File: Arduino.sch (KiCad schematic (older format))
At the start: 0 parts

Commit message: Add projects simples and adding a sun Sch
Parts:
- added BT?: Battery, symbol Device:Battery
- added C? (x2): C, symbol Device:C
- added C?: CP, symbol Device:CP
- added D?: LED, symbol Device:LED
- added R? (x2): R, symbol Device:R
- added U?: 24LC1025, symbol Memory_EEPROM:24LC1025
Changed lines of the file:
@@
 $Descr A4 11693 8268
 encoding utf-8
-Sheet 1 1
+Sheet 1 2
 Title "Arduino"
 Date "2021-10-07"
@@
 Comment4 ""
 $EndDescr
+$Comp
+L Device:Battery BT?
+U 1 1 615F0300
+P 7050 3050
+F 0 "BT?" H 7158 3096 50  0000 L CNN
+F 1 "Battery" H 7158 3005 50  0000 L CNN
+F 2 "" V 7050 3110 50  0001 C CNN
+F 3 "~" V 7050 3110 50  0001 C CNN
+	1    7050 3050
+	1    0    0    -1
+$EndComp
+$Comp
+L Device:C C?
+U 1 1 615F14AB
+P 5450 1750
+F 0 "C?" H 5565 1796 50  0000 L CNN
+F 1 "C" H 5565 1705 50  0000 L CNN
+F 2 "" H 5488 1600 50  0001 C CNN
+F 3 "~" H 5450 1750 50  0001 C CNN
+	1    5450 1750
+	1    0    0    -1
+$EndComp
+$Comp
+L Device:C C?
+U 1 1 615F1778
+P 5450 2400
+F 0 "C?" H 5565 2446 50  0000 L CNN
+F 1 "C" H 5565 2355 50  0000 L CNN
+F 2 "" H 5488 2250 50  0001 C CNN
+F 3 "~" H 5450 2400 50  0001 C CNN
+	1    5450 2400
+	1    0    0    -1
+$EndComp
+$Comp
+L Device:CP C?
+U 1 1 615F1B97
+P 6350 1800
+F 0 "C?" H 6468 1846 50  0000 L CNN
+F 1 "CP" H 6468 1755 50  0000 L CNN
+F 2 "" H 6388 1650 50  0001 C CNN
+F 3 "~" H 6350 1800 50  0001 C CNN
+	1    6350 1800
+	1    0    0    -1
+$EndComp
+$Comp
+L Device:LED D?
+U 1 1 615F28FB
+P 7600 1750
+F 0 "D?" H 7593 1967 50  0000 C CNN
+F 1 "LED" H 7593 1876 50  0000 C CNN
+F 2 "" H 7600 1750 50  0001 C CNN
+F 3 "~" H 7600 1750 50  0001 C CNN
+	1    7600 1750
+	1    0    0    -1
+$EndComp
+$Comp
+L Device:R R?
+U 1 1 615F2E86
+P 8250 1950
+F 0 "R?" H 8320 1996 50  0000 L CNN
+F 1 "R" H 8320 1905 50  0000 L CNN
+F 2 "" V 8180 1950 50  0001 C CNN
+F 3 "~" H 8250 1950 50  0001 C CNN
+	1    8250 1950
+	1    0    0    -1
+$EndComp
+$Comp
+L Device:R R?
+U 1 1 615F3234
+P 8250 2400
+F 0 "R?" H 8320 2446 50  0000 L CNN
+F 1 "R" H 8320 2355 50  0000 L CNN
+F 2 "" V 8180 2400 50  0001 C CNN
+F 3 "~" H 8250 2400 50  0001 C CNN
+	1    8250 2400
+	1    0    0    -1
+$EndComp
+$Comp
+L Memory_EEPROM:24LC1025 U?
+U 1 1 615F39A8
+P 9550 1950
+F 0 "U?" H 9550 2431 50  0000 C CNN
+F 1 "24LC1025" H 9550 2340 50  0000 C CNN
+F 2 "" H 9550 1950 50  0001 C CNN
+F 3 "http://ww1.microchip.com/downloads/en/DeviceDoc/21941B.pdf" H 9550 1950 50  0001 C CNN
+	1    9550 1950
+	1    0    0    -1
+$EndComp
+$Sheet
+S 8250 3000 2950 3550
+U 615F48EA
+F0 "Connectors" 50
+F1 "connectors.sch" 50
+$EndSheet
 $EndSCHEMATC

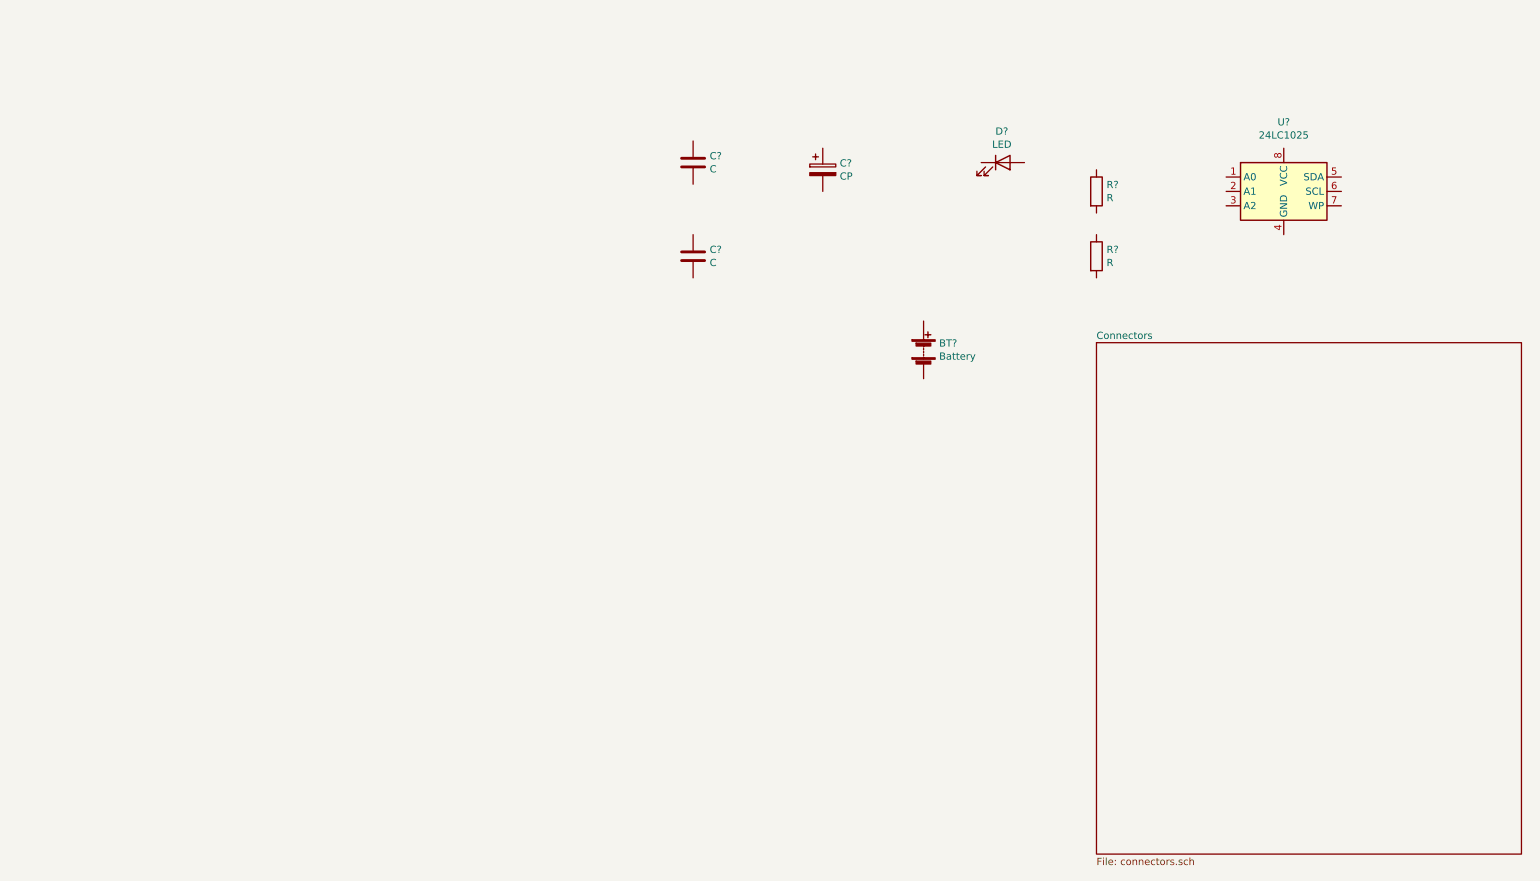
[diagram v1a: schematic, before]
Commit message: Complete the association with footprint
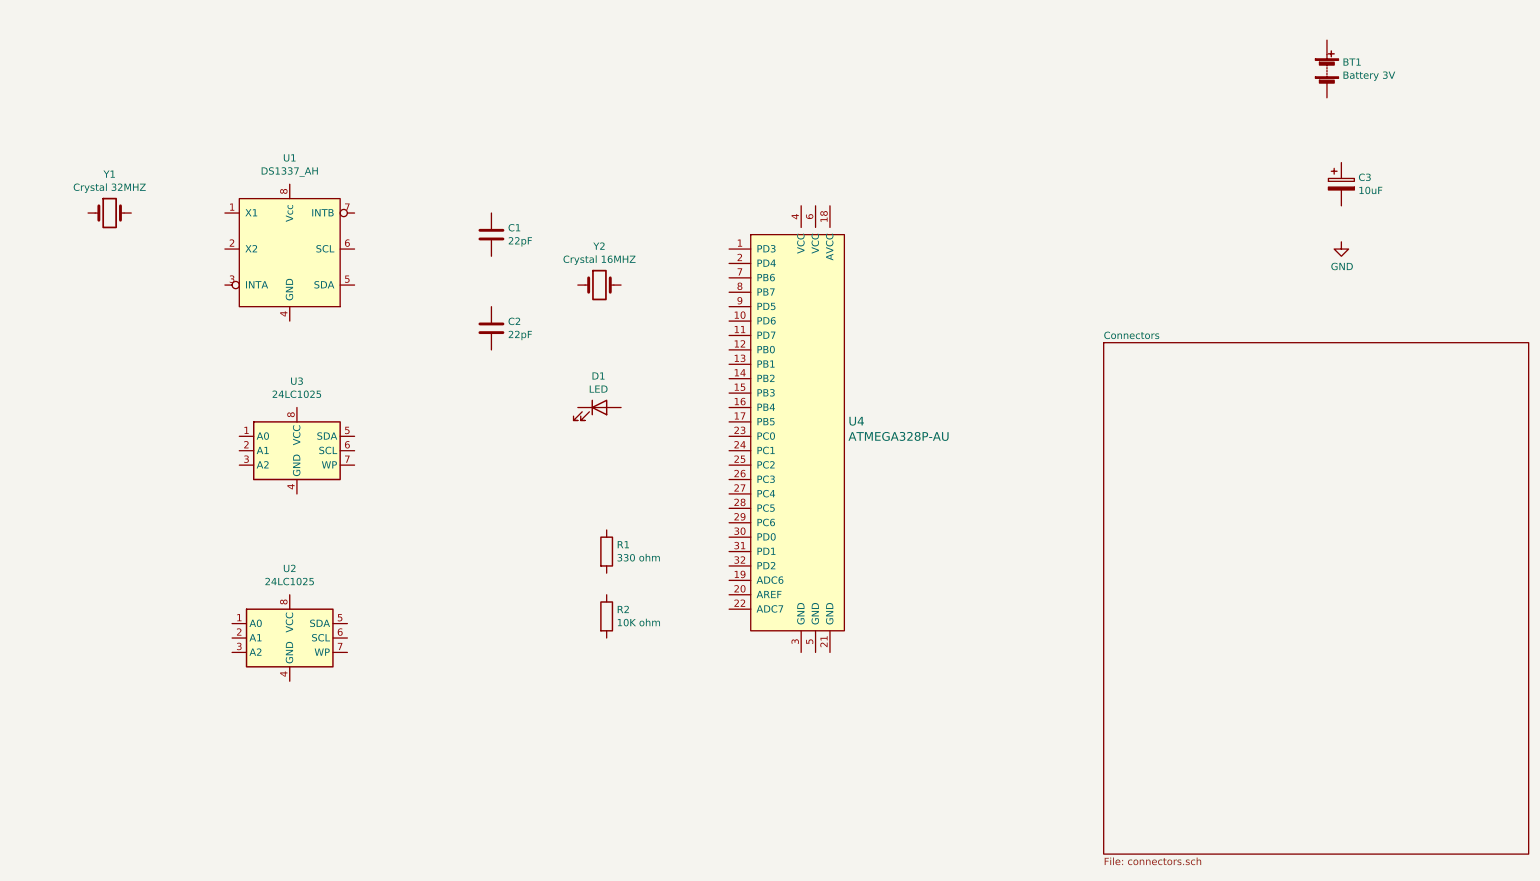
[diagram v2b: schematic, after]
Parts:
- added U1: DS1337_AH, Package_SO:SO-8_5.3x6.2mm_P1.27mm, symbol Ahmad_Library:DS1337_AH
- added U2: 24LC1025, Package_SO:SOIC-8_5.23x5.23mm_P1.27mm, symbol Memory_EEPROM:24LC1025
- added U4: ATMEGA328P-AU, digikey-footprints:TQFP-32_7x7mm, symbol dk_Embedded-Microcontrollers:ATMEGA328P-AU
- added Y1: Crystal 32MHZ, Crystal:Crystal_SMD_MicroCrystal_CC7V-T1A-2Pin_3.2x1.5mm, symbol Device:Crystal
- added Y2: Crystal 16MHZ, Crystal:Crystal_SMD_5032-2Pin_5.0x3.2mm_HandSoldering, symbol Device:Crystal
- BT1: renamed from BT?; value Battery -> Battery 3V; footprint (none) -> Connector_PinHeader_2.54mm:PinHeader_1x02_P2.54mm_Vertical
- C1, C2: renamed from C?; value C -> 22pF; footprint (none) -> Capacitor_SMD:C_0805_2012Metric_Pad1.18x1.45mm_HandSolder
- C3: renamed from C?; value CP -> 10uF; footprint (none) -> Capacitor_SMD:C_0805_2012Metric_Pad1.18x1.45mm_HandSolder
- D1: renamed from D?; footprint (none) -> LED_SMD:LED_0805_2012Metric_Pad1.15x1.40mm_HandSolder
- R1: renamed from R?; value R -> 330 ohm; footprint (none) -> Resistor_SMD:R_0805_2012Metric_Pad1.20x1.40mm_HandSolder
- R2: renamed from R?; value R -> 10K ohm; footprint (none) -> Resistor_SMD:R_0805_2012Metric_Pad1.20x1.40mm_HandSolder
- U3: renamed from U?; footprint (none) -> Package_SO:SOIC-8_5.23x5.23mm_P1.27mm
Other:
- moved on the sheet: BT1, C1, C2, C3, D1, R1, R2, U3
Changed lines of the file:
@@
 $EndDescr
 $Comp
-L Device:Battery BT?
+L Device:Battery BT1
 U 1 1 615F0300
-P 7050 3050
-F 0 "BT?" H 7158 3096 50  0000 L CNN
-F 1 "Battery" H 7158 3005 50  0000 L CNN
-F 2 "" V 7050 3110 50  0001 C CNN
-F 3 "~" V 7050 3110 50  0001 C CNN
-	1    7050 3050
+P 9850 1100
+F 0 "BT1" H 9958 1146 50  0000 L CNN
+F 1 "Battery 3V" H 9958 1055 50  0000 L CNN
+F 2 "Connector_PinHeader_2.54mm:PinHeader_1x02_P2.54mm_Vertical" V 9850 1160 50  0001 C CNN
+F 3 "~" V 9850 1160 50  0001 C CNN
+	1    9850 1100
 	1    0    0    -1
 $EndComp
 $Comp
-L Device:C C?
+L Device:C C1
 U 1 1 615F14AB
-P 5450 1750
-F 0 "C?" H 5565 1796 50  0000 L CNN
-F 1 "C" H 5565 1705 50  0000 L CNN
-F 2 "" H 5488 1600 50  0001 C CNN
-F 3 "~" H 5450 1750 50  0001 C CNN
-	1    5450 1750
+P 4050 2250
+F 0 "C1" H 4165 2296 50  0000 L CNN
+F 1 "22pF" H 4165 2205 50  0000 L CNN
+F 2 "Capacitor_SMD:C_0805_2012Metric_Pad1.18x1.45mm_HandSolder" H 4088 2100 50  0001 C CNN
+F 3 "~" H 4050 2250 50  0001 C CNN
+	1    4050 2250
 	1    0    0    -1
 $EndComp
 $Comp
-L Device:C C?
+L Device:C C2
 U 1 1 615F1778
-P 5450 2400
-F 0 "C?" H 5565 2446 50  0000 L CNN
-F 1 "C" H 5565 2355 50  0000 L CNN
-F 2 "" H 5488 2250 50  0001 C CNN
-F 3 "~" H 5450 2400 50  0001 C CNN
-	1    5450 2400
+P 4050 2900
+F 0 "C2" H 4165 2946 50  0000 L CNN
+F 1 "22pF" H 4165 2855 50  0000 L CNN
+F 2 "Capacitor_SMD:C_0805_2012Metric_Pad1.18x1.45mm_HandSolder" H 4088 2750 50  0001 C CNN
+F 3 "~" H 4050 2900 50  0001 C CNN
+	1    4050 2900
 	1    0    0    -1
 $EndComp
 $Comp
-L Device:CP C?
+L Device:CP C3
 U 1 1 615F1B97
-P 6350 1800
-F 0 "C?" H 6468 1846 50  0000 L CNN
-F 1 "CP" H 6468 1755 50  0000 L CNN
-F 2 "" H 6388 1650 50  0001 C CNN
-F 3 "~" H 6350 1800 50  0001 C CNN
-	1    6350 1800
+P 9950 1900
+F 0 "C3" H 10068 1946 50  0000 L CNN
+F 1 "10uF" H 10068 1855 50  0000 L CNN
+F 2 "Capacitor_SMD:C_0805_2012Metric_Pad1.18x1.45mm_HandSolder" H 9988 1750 50  0001 C CNN
+F 3 "~" H 9950 1900 50  0001 C CNN
+	1    9950 1900
 	1    0    0    -1
 $EndComp
 $Comp
-L Device:LED D?
+L Device:LED D1
 U 1 1 615F28FB
-P 7600 1750
-F 0 "D?" H 7593 1967 50  0000 C CNN
-F 1 "LED" H 7593 1876 50  0000 C CNN
-F 2 "" H 7600 1750 50  0001 C CNN
-F 3 "~" H 7600 1750 50  0001 C CNN
-	1    7600 1750
+P 4800 3450
+F 0 "D1" H 4793 3667 50  0000 C CNN
+F 1 "LED" H 4793 3576 50  0000 C CNN
+F 2 "LED_SMD:LED_0805_2012Metric_Pad1.15x1.40mm_HandSolder" H 4800 3450 50  0001 C CNN
+F 3 "~" H 4800 3450 50  0001 C CNN
+	1    4800 3450
 	1    0    0    -1
 $EndComp
 $Comp
-L Device:R R?
-U 1 1 615F2E86
-P 8250 1950
-F 0 "R?" H 8320 1996 50  0000 L CNN
-F 1 "R" H 8320 1905 50  0000 L CNN
-F 2 "" V 8180 1950 50  0001 C CNN
-F 3 "~" H 8250 1950 50  0001 C CNN
-	1    8250 1950
-	1    0    0    -1
-$EndComp
-$Comp
-L Device:R R?
-U 1 1 615F3234
-P 8250 2400
-F 0 "R?" H 8320 2446 50  0000 L CNN
-F 1 "R" H 8320 2355 50  0000 L CNN
-F 2 "" V 8180 2400 50  0001 C CNN
-F 3 "~" H 8250 2400 50  0001 C CNN
-	1    8250 2400
-	1    0    0    -1
-$EndComp
-$Comp
-L Memory_EEPROM:24LC1025 U?
+L Memory_EEPROM:24LC1025 U3
 U 1 1 615F39A8
-P 9550 1950
-F 0 "U?" H 9550 2431 50  0000 C CNN
-F 1 "24LC1025" H 9550 2340 50  0000 C CNN
-F 2 "" H 9550 1950 50  0001 C CNN
-F 3 "http://ww1.microchip.com/downloads/en/DeviceDoc/21941B.pdf" H 9550 1950 50  0001 C CNN
-	1    9550 1950
+P 2700 3750
+F 0 "U3" H 2700 4231 50  0000 C CNN
+F 1 "24LC1025" H 2700 4140 50  0000 C CNN
+F 2 "Package_SO:SOIC-8_5.23x5.23mm_P1.27mm" H 2700 3750 50  0001 C CNN
+F 3 "http://ww1.microchip.com/downloads/en/DeviceDoc/21941B.pdf" H 2700 3750 50  0001 C CNN
+	1    2700 3750
 	1    0    0    -1
 $EndComp
 $Sheet
-S 8250 3000 2950 3550
+S 8300 3000 2950 3550
 U 615F48EA
 F0 "Connectors" 50
 F1 "connectors.sch" 50
 $EndSheet
+$Comp
+L Ahmad_Library:DS1337_AH U?
+U 1 1 61601E43
+P 2650 2350
+AR Path="/615F48EA/61601E43" Ref="U?"  Part="1"
+AR Path="/61601E43" Ref="U1"  Part="1"
+F 0 "U1" H 2650 2981 50  0000 C CNN
+F 1 "DS1337_AH" H 2650 2890 50  0000 C CNN
+F 2 "Package_SO:SO-8_5.3x6.2mm_P1.27mm" H 2650 3000 50  0001 C CNN
+F 3 "" H 2650 3000 50  0001 C CNN
+	1    2650 2350
+	1    0    0    -1
+$EndComp
+$Comp
+L Device:Crystal Y?
+U 1 1 61601E49
+P 1400 2100
+AR Path="/615F48EA/61601E49" Ref="Y?"  Part="1"
+AR Path="/61601E49" Ref="Y1"  Part="1"
+F 0 "Y1" H 1400 2368 50  0000 C CNN
+F 1 "Crystal 32MHZ" H 1400 2277 50  0000 C CNN
+F 2 "Crystal:Crystal_SMD_MicroCrystal_CC7V-T1A-2Pin_3.2x1.5mm" H 1400 2100 50  0001 C CNN
+F 3 "~" H 1400 2100 50  0001 C CNN
+	1    1400 2100
+	1    0    0    -1
+$EndComp
+$Comp
+L Device:Crystal Y?
+U 1 1 61601E4F
+P 4800 2600
+AR Path="/615F48EA/61601E4F" Ref="Y?"  Part="1"
+AR Path="/61601E4F" Ref="Y2"  Part="1"
+F 0 "Y2" H 4800 2868 50  0000 C CNN
+F 1 "Crystal  16MHZ" H 4800 2777 50  0000 C CNN
+F 2 "Crystal:Crystal_SMD_5032-2Pin_5.0x3.2mm_HandSoldering" H 4800 2600 50  0001 C CNN
+F 3 "~" H 4800 2600 50  0001 C CNN
+	1    4800 2600
+	1    0    0    -1
+$EndComp
+$Comp
+L Memory_EEPROM:24LC1025 U2
+U 1 1 616045B6
+P 2650 5050
+F 0 "U2" H 2650 5531 50  0000 C CNN
+F 1 "24LC1025" H 2650 5440 50  0000 C CNN
+F 2 "Package_SO:SOIC-8_5.23x5.23mm_P1.27mm" H 2650 5050 50  0001 C CNN
+F 3 "http://ww1.microchip.com/downloads/en/DeviceDoc/21941B.pdf" H 2650 5050 50  0001 C CNN
+	1    2650 5050
+	1    0    0    -1
+$EndComp
+$Comp
+L dk_Embedded-Microcontrollers:ATMEGA328P-AU U?
+U 1 1 61601E3D
+P 6200 3650
+AR Path="/615F48EA/61601E3D" Ref="U?"  Part="1"
+AR Path="/61601E3D" Ref="U4"  Part="1"
+F 0 "U4" H 6528 3753 60  0000 L CNN
+F 1 "ATMEGA328P-AU" H 6528 3647 60  0000 L CNN
+F 2 "digikey-footprints:TQFP-32_7x7mm" H 6400 3850 60  0001 L CNN
+F 3 "http://www.microchip.com/mymicrochip/filehandler.aspx?ddocname=en608326" H 6400 3950 60  0001 L CNN
+F 4 "ATMEGA328P-AU-ND" H 6400 4050 60  0001 L CNN "Digi-Key_PN"
+F 5 "ATMEGA328P-AU" H 6400 4150 60  0001 L CNN "MPN"
+F 6 "Integrated Circuits (ICs)" H 6400 4250 60  0001 L CNN "Category"
+F 7 "Embedded - Microcontrollers" H 6400 4350 60  0001 L CNN "Family"
+F 8 "http://www.microchip.com/mymicrochip/filehandler.aspx?ddocname=en608326" H 6400 4450 60  0001 L CNN "DK_Datasheet_Link"
+F 9 "/product-detail/en/microchip-technology/ATMEGA328P-AU/ATMEGA328P-AU-ND/1832260" H 6400 4550 60  0001 L CNN "DK_Detail_Page"
+F 10 "IC MCU 8BIT 32KB FLASH 32TQFP" H 6400 4650 60  0001 L CNN "Description"
+F 11 "Microchip Technology" H 6400 4750 60  0001 L CNN "Manufacturer"
+F 12 "Active" H 6400 4850 60  0001 L CNN "Status"
+	1    6200 3650
+	1    0    0    -1
+$EndComp
+$Comp
+L Device:R R2
+U 1 1 615F3234
+P 4850 4900
+F 0 "R2" H 4920 4946 50  0000 L CNN
+F 1 "10K ohm" H 4920 4855 50  0000 L CNN
+F 2 "Resistor_SMD:R_0805_2012Metric_Pad1.20x1.40mm_HandSolder" V 4780 4900 50  0001 C CNN
+F 3 "~" H 4850 4900 50  0001 C CNN
+	1    4850 4900
+	1    0    0    -1
+$EndComp
+$Comp
+L Device:R R1
+U 1 1 615F2E86
+P 4850 4450
+F 0 "R1" H 4920 4496 50  0000 L CNN
+F 1 "330 ohm" H 4920 4405 50  0000 L CNN
+F 2 "Resistor_SMD:R_0805_2012Metric_Pad1.20x1.40mm_HandSolder" V 4780 4450 50  0001 C CNN
+F 3 "~" H 4850 4450 50  0001 C CNN
+	1    4850 4450
+	1    0    0    -1
+$EndComp
+$Comp
+L power:GND #PWR01
+U 1 1 61618778
+P 9950 2300
+F 0 "#PWR01" H 9950 2050 50  0001 C CNN
+F 1 "GND" H 9955 2127 50  0000 C CNN
+F 2 "" H 9950 2300 50  0001 C CNN
+F 3 "" H 9950 2300 50  0001 C CNN
+	1    9950 2300
+	1    0    0    -1
+$EndComp
 $EndSCHEMATC

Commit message: Completed the connection in the connectors sheet
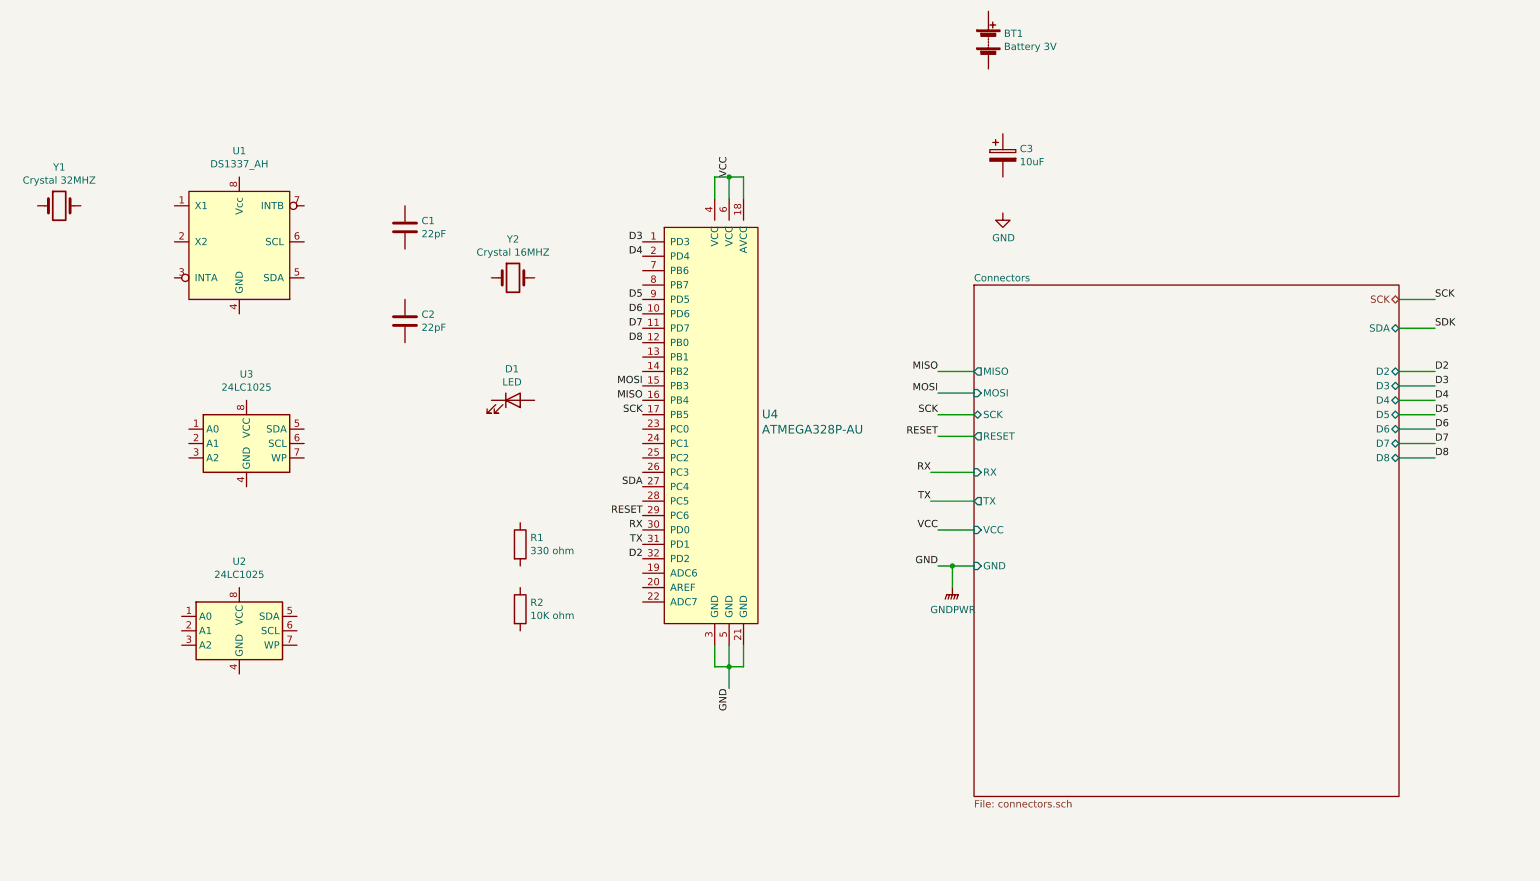
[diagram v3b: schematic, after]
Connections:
- net GND: now also U4.21 (GND), U4.3 (GND), U4.5 (GND)
- net D3: now reaches U4.1 (PD3)
- net D6: now reaches U4.10 (PD6)
- net D7: now reaches U4.11 (PD7)
- net D8: now reaches U4.12 (PB0)
- net MOSI: now reaches U4.15 (PB3)
- net MISO: now reaches U4.16 (PB4)
- net SCK: now reaches U4.17 (PB5)
- net VCC: now reaches U4.18 (AVCC)
- net VCC: now also U4.4 (VCC), U4.6 (VCC)
- net D4: now reaches U4.2 (PD4)
- net SDA: now reaches U4.27 (PC4)
- net RESET: now reaches U4.29 (PC6)
- net RX: now reaches U4.30 (PD0)
- net TX: now reaches U4.31 (PD1)
- net D2: now reaches U4.32 (PD2)
- net D5: now reaches U4.9 (PD5)
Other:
- moved on the sheet: BT1, C1, C2, C3, D1, R1, R2, U1, U2, U3, U4, Y1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
